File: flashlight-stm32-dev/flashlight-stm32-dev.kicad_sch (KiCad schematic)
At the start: 88 parts, among them J1 USB_C_Receptacle, J2 ST-LINK, Q1 2N7002H, Q2 2N7002H, Q3 2N7002H, SW1 RESET, SW2 BOOT, U1 BQ25185DLHR, U2 STM32L151C8Tx, U3 BMA400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

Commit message: with headers
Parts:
- added J3: IO1, Connector_PinHeader_2.54mm:PinHeader_1x11_P2.54mm_Vertical, symbol Connector:Conn_01x11_Pin
- added J4: IO2, Connector_PinHeader_2.54mm:PinHeader_1x11_P2.54mm_Vertical, symbol Connector:Conn_01x11_Pin
- added JP1: Jumper_2_Bridged, Jumper:SolderJumper-2_P1.3mm_Bridged_RoundedPad1.0x1.5mm, symbol Jumper:Jumper_2_Bridged
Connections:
- net +3.3V: now also J3.10 (Pin_10), J4.1 (Pin_1)
- net GND: now also J3.11 (Pin_11), J4.2 (Pin_2), JP1.1 (A)
- net GNDA: now also JP1.2 (B)
- net PA1: now reaches U2.11 (PA1)
- net PA1: now also J3.1 (Pin_1)
- net PA2: now reaches U2.12 (PA2)
- net PA2: now also J3.2 (Pin_2)
- net PA3: now reaches U2.13 (PA3)
- net PA3: now also J3.3 (Pin_3)
- net PA4: now reaches U2.14 (PA4)
- net PA4: now also J3.4 (Pin_4)
- net PA5: now reaches U2.15 (PA5)
- net PA5: now also J3.5 (Pin_5)
- net PA6: now reaches U2.16 (PA6)
- net PA6: now also J3.6 (Pin_6)
- net PA7: now reaches U2.17 (PA7)
- net PA7: now also J3.7 (Pin_7)
- net PB10: now reaches U2.21 (PB10)
- net PB10: now also J3.8 (Pin_8)
- net PB11: now reaches U2.22 (PB11)
- net PB11: now also J3.9 (Pin_9)
- net PB12: now reaches U2.25 (PB12)
- net PB12: now also J4.11 (Pin_11)
- net PB13: now reaches U2.26 (PB13)
- net PB13: now also J4.10 (Pin_10)
- net PB14: now reaches U2.27 (PB14)
- net PB14: now also J4.9 (Pin_9)
- net PB15: now reaches U2.28 (PB15)
- net PB15: now also J4.8 (Pin_8)
- net PA8: now reaches U2.29 (PA8)
- net PA8: now also J4.7 (Pin_7)
- net PA9: now reaches U2.30 (PA9)
- net PA9: now also J4.6 (Pin_6)
- net PA10: now reaches U2.31 (PA10)
- net PA10: now also J4.5 (Pin_5)
- net PA15: now reaches U2.38 (PA15)
- net PA15: now also J4.4 (Pin_4)
- net PB3: now reaches U2.39 (PB3)
- net PB3: now also J4.3 (Pin_3)
- no-connect marks 31 -> 13
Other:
- moved on the sheet: J2

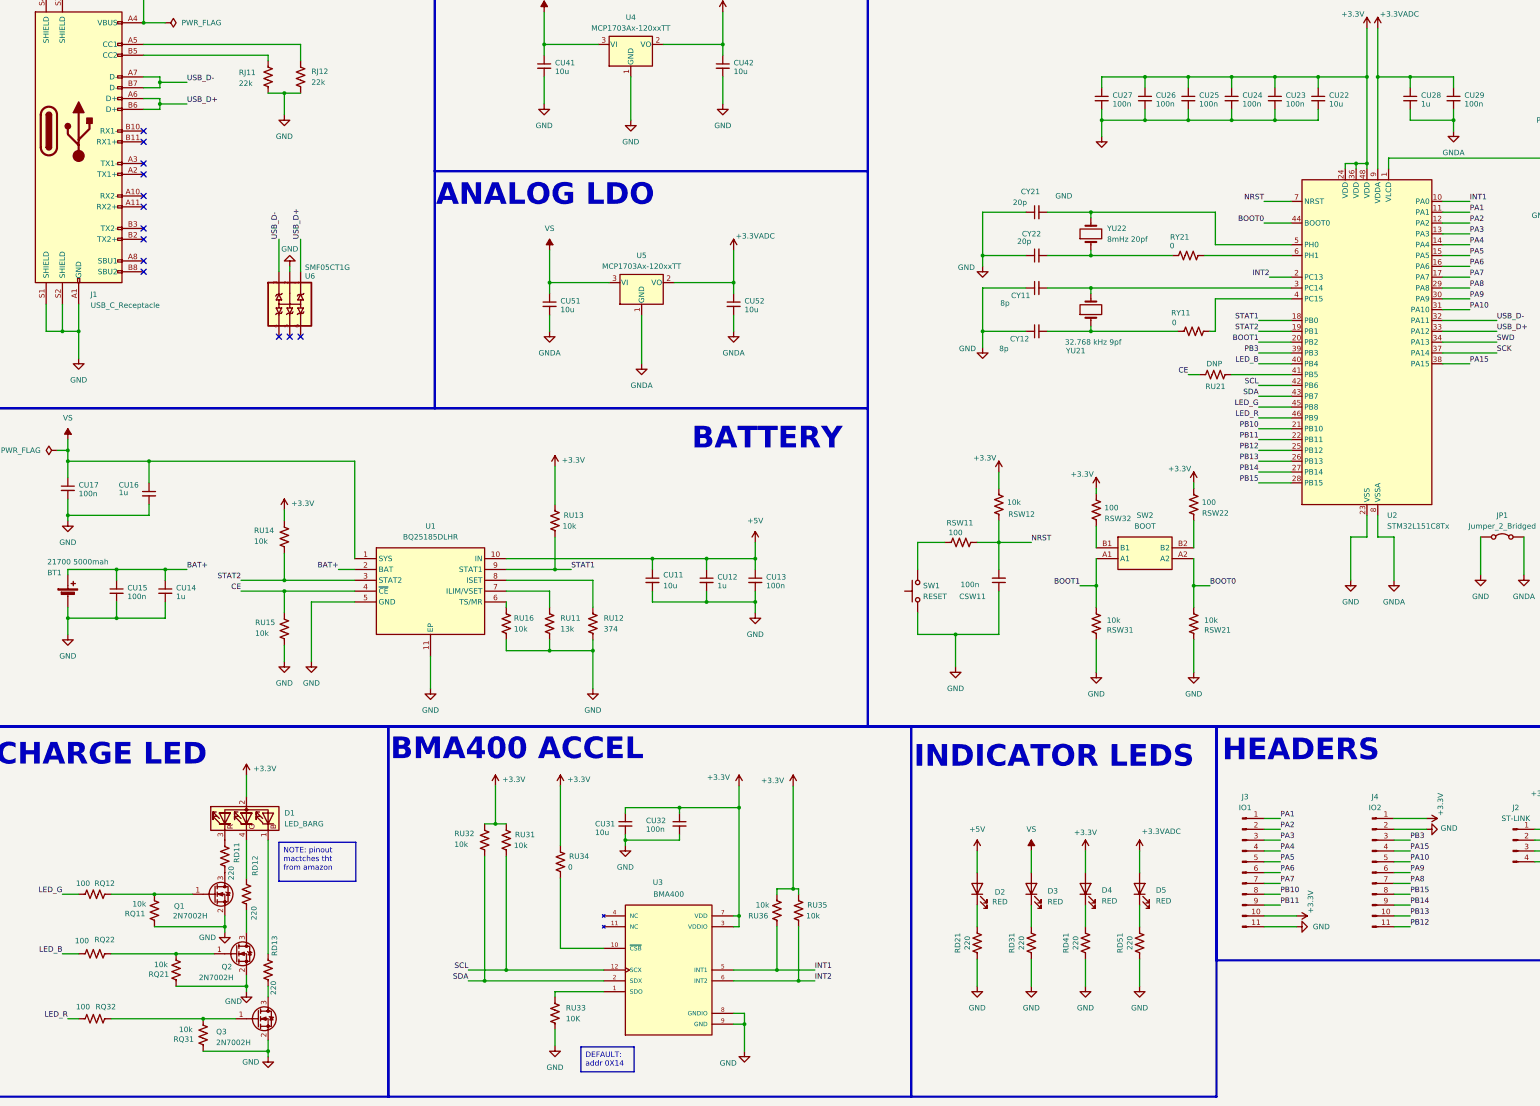
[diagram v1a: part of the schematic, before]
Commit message: updated accel and usbc cc
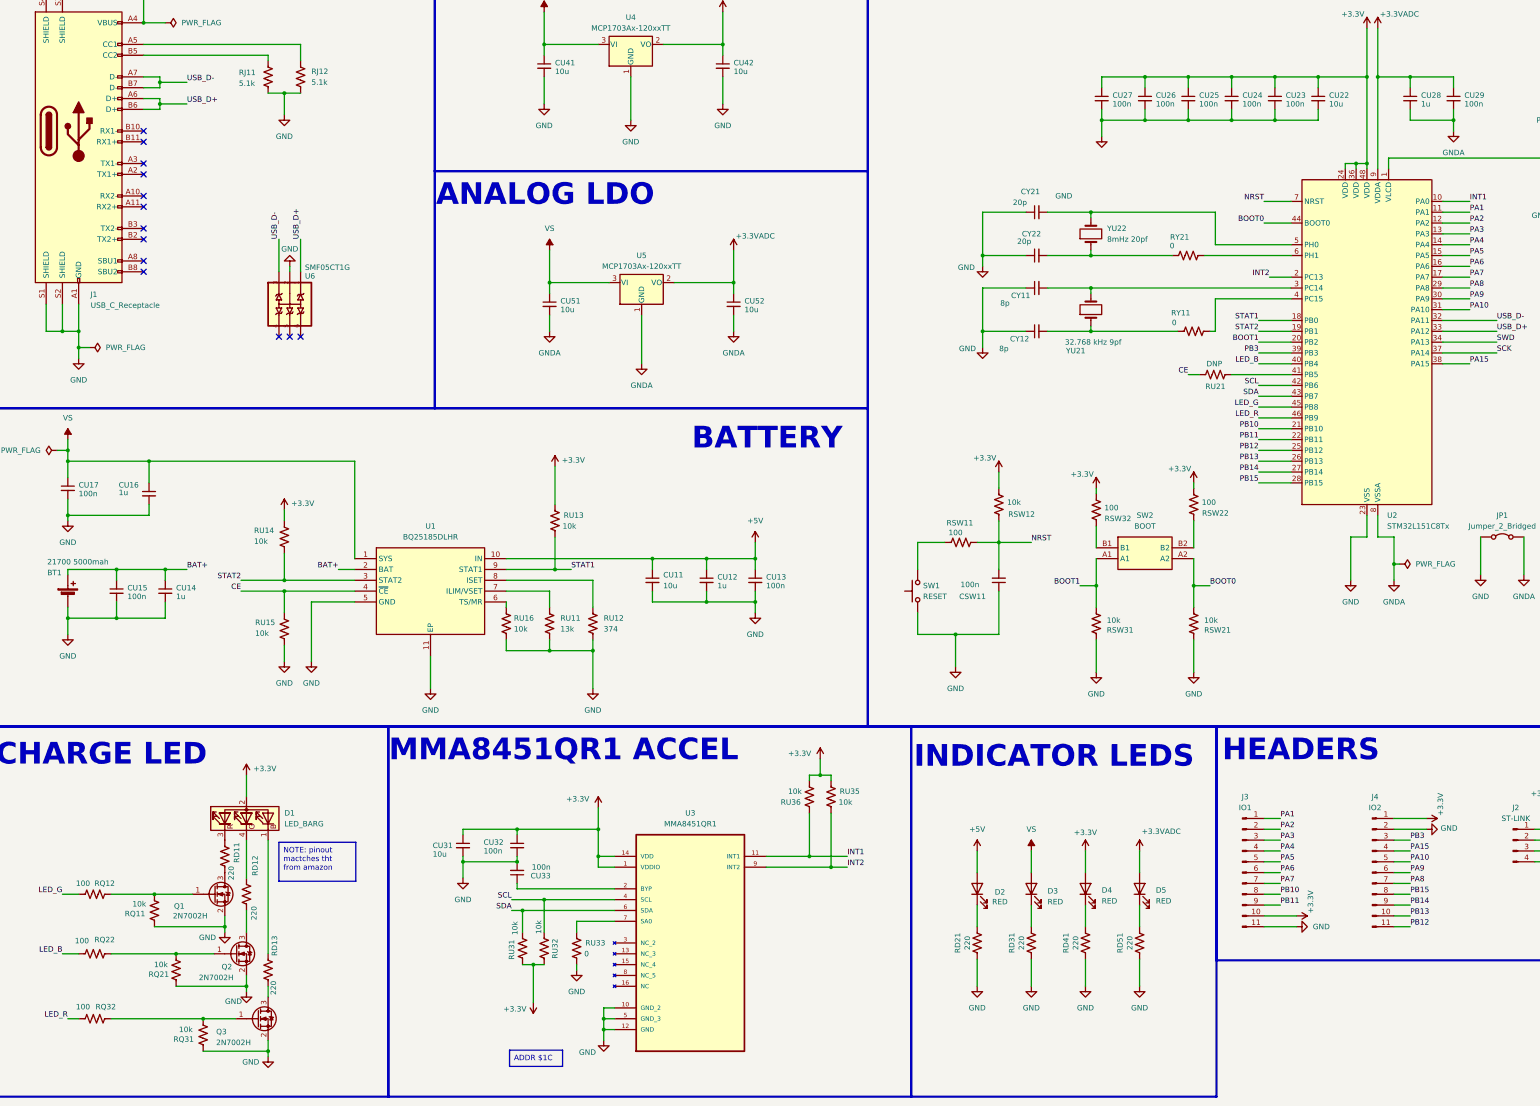
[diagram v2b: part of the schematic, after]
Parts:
- removed RU33: 10K, Resistor_SMD:R_0603_1608Metric_Pad0.98x0.95mm_HandSolder, symbol Device:R_US
- removed U3: BMA400, BMA400:XDCR_BMA400, symbol BMA400:BMA400
- added CU33: 100n, Capacitor_SMD:C_0402_1005Metric, symbol Device:C_Small
- added U3: MMA8451QR1, MMA8451QR1:QFN50P300X300X100-16N, symbol MMA8451QR1:MMA8451QR1
- RJ11, RJ12: value 22k -> 5.1k
- renumbered RU34 to RU33
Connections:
- net +3.3V: now also U3.1 (VDDIO), U3.14 (VDD); no longer RU33.2
- net GND: now also RU33.1, CU33.2, U3.10 (GND_2), U3.12 (GND), U3.5 (GND_3)
- net INT1: now also U3.11 (INT1)
- net INT2: now also U3.9 (INT2)
- net SCL: now also RU32.1, U3.4 (SCL); no longer RU31.1
- net SDA: now also RU31.1, U3.6 (SDA); no longer RU32.1
- new net: CU33.1, U3.2 (BYP)
- new net: RU33.2, U3.7 (SA0)
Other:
- note added: "MMA8451QR1 ACCEL"
- note removed: "BMA400 ACCEL"
- moved on the sheet: CU31, CU32, RU31, RU32, RU33, RU35, RU36
